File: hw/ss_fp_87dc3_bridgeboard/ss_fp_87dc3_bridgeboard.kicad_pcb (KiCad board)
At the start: 2 copper layers, 50 x 20 mm, 16 parts, among them J101 Conn_01x02, J102 Conn_01x04, J103 Conn_01x03, J104 Conn_01x02, J105 Conn_01x04, J106 Conn_01x03, J107 Conn_01x02, J108 Conn_01x04, J109 Conn_01x02, J110 Conn_01x04, J111 Conn_01x03, J112 Conn_01x03

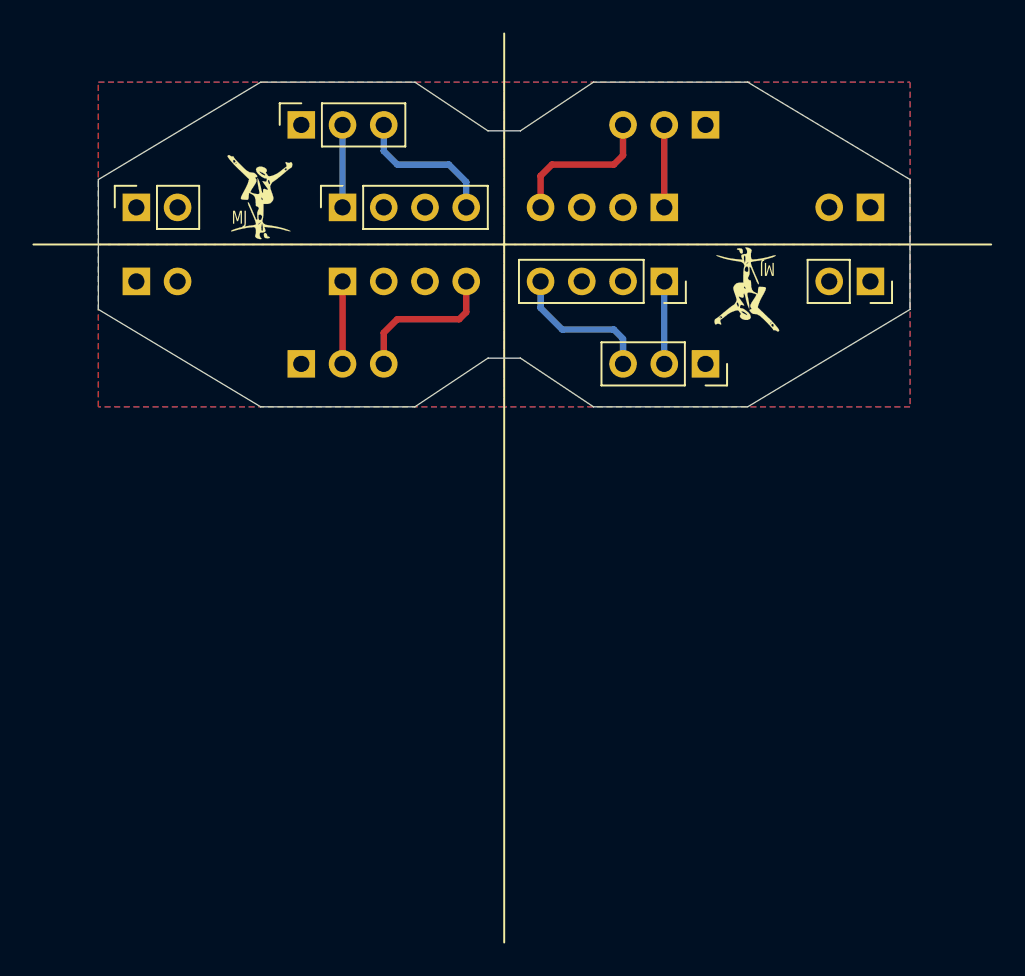
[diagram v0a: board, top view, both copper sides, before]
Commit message: Adjust separate bridge-board panel for potential production (R1A *not* ordered though)
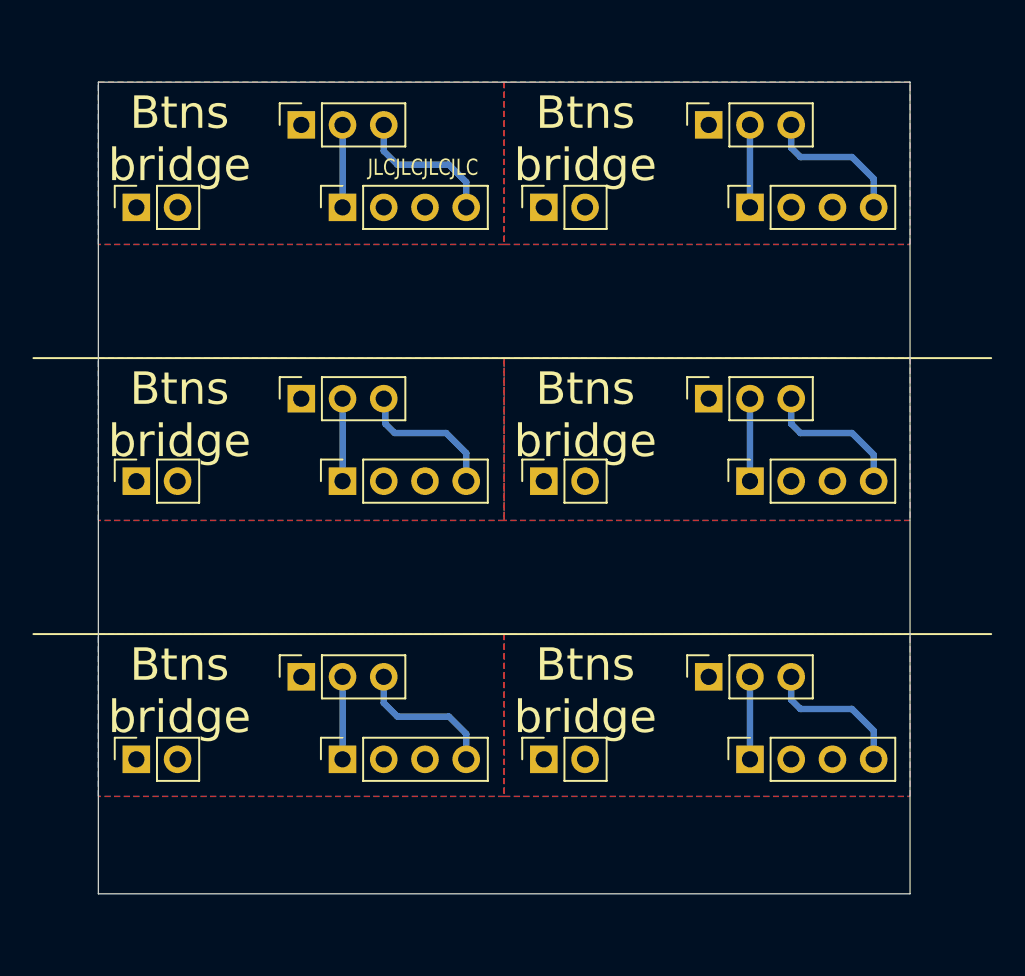
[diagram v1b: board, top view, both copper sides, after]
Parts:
- added J113: Conn_01x02, Connector_PinSocket_2.54mm:PinSocket_1x02_P2.54mm_Vertical, F.Cu at (102.3, 91.7)
- added J114: Conn_01x04, Connector_PinSocket_2.54mm:PinSocket_1x04_P2.54mm_Vertical, F.Cu at (115.0, 91.7)
- added J115: Conn_01x02, Connector_PinSocket_2.54mm:PinSocket_1x02_P2.54mm_Vertical, F.Cu at (127.4, 91.7)
- added J116: Conn_01x04, Connector_PinSocket_2.54mm:PinSocket_1x04_P2.54mm_Vertical, F.Cu at (140.1, 91.7)
- added J117: Conn_01x03, Connector_PinSocket_2.54mm:PinSocket_1x03_P2.54mm_Vertical, F.Cu at (112.5, 86.6)
- added J118: Conn_01x03, Connector_PinSocket_2.54mm:PinSocket_1x03_P2.54mm_Vertical, F.Cu at (137.6, 86.6)
- added Logo105: Logo_MJ, customlib_mj_fp:MJ_Mini, B.Cu at (135.0, 91.0)
- added Logo106: Logo_MJ, customlib_mj_fp:MJ_Mini, B.Cu at (110.0, 91.0)
- J104, J105, J106, J107, J108, J111: moved to F.Cu
- Logo101, Logo104: moved to B.Cu
- moved Logo104 32.0 mm to (110.0, 74.0)
- moved Logo102 29.9 mm to (110.0, 57.0)
- moved Logo103 27.4 mm to (135.0, 74.0), turned to 180 degrees
- moved Logo101 25.0 mm to (135.0, 57.0), turned to 180 degrees
- moved J109 23.6 mm to (127.4, 74.6), turned to 90 degrees
- moved J104 20.1 mm to (127.4, 57.7)
- moved J110 13.4 mm to (140.1, 74.6), turned to 90 degrees
- moved J107 12.3 mm to (102.3, 74.6), turned to 90 degrees
- moved J108 12.3 mm to (115.0, 74.6), turned to 90 degrees
- moved J105 5.28 mm to (140.1, 57.7)
- moved J112 2.15 mm to (137.6, 69.5), turned to 90 degrees
- moved J111 2.14 mm to (112.5, 69.5), turned to 90 degrees
- moved J106 0.20 mm to (137.6, 52.6)
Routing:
- net Net-(J114-Pad4): track 0.00 -> 9.04 mm
- net Net-(J116-Pad4): track 0.00 -> 9.04 mm
- net Net-(J116-Pad1): track 0.00 -> 5.08 mm
- net Net-(J114-Pad1): track 0.00 -> 5.08 mm
- added copper zone on B.Cu, net /COM_5
- added copper zone on F.Cu, net /COM_5
- added copper zone on B.Cu, net /COM_6
- added copper zone on F.Cu, net /COM_6
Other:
- board size 50 x 20 mm -> 50 x 50 mm
- board text added: "Btns bridge"
- board text added: "JLCJLCJLCJLC"

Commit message: Kicad 6.0 : Most of SS2k & subprojects updated to kicad6 The projects should from now on be opened through the .kicad_pro files instead of .pro, etc. NOTE: Kicad 6 is now used. Kicad5 is NOT able to open v6+ files.
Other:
- net class Default removed
